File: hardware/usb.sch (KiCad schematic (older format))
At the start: 33 parts, among them J2 USB_B_Micro, U14 FT2232H, U31 93LCxxB, Y1 ABM10-167-12.000MHZ-T3

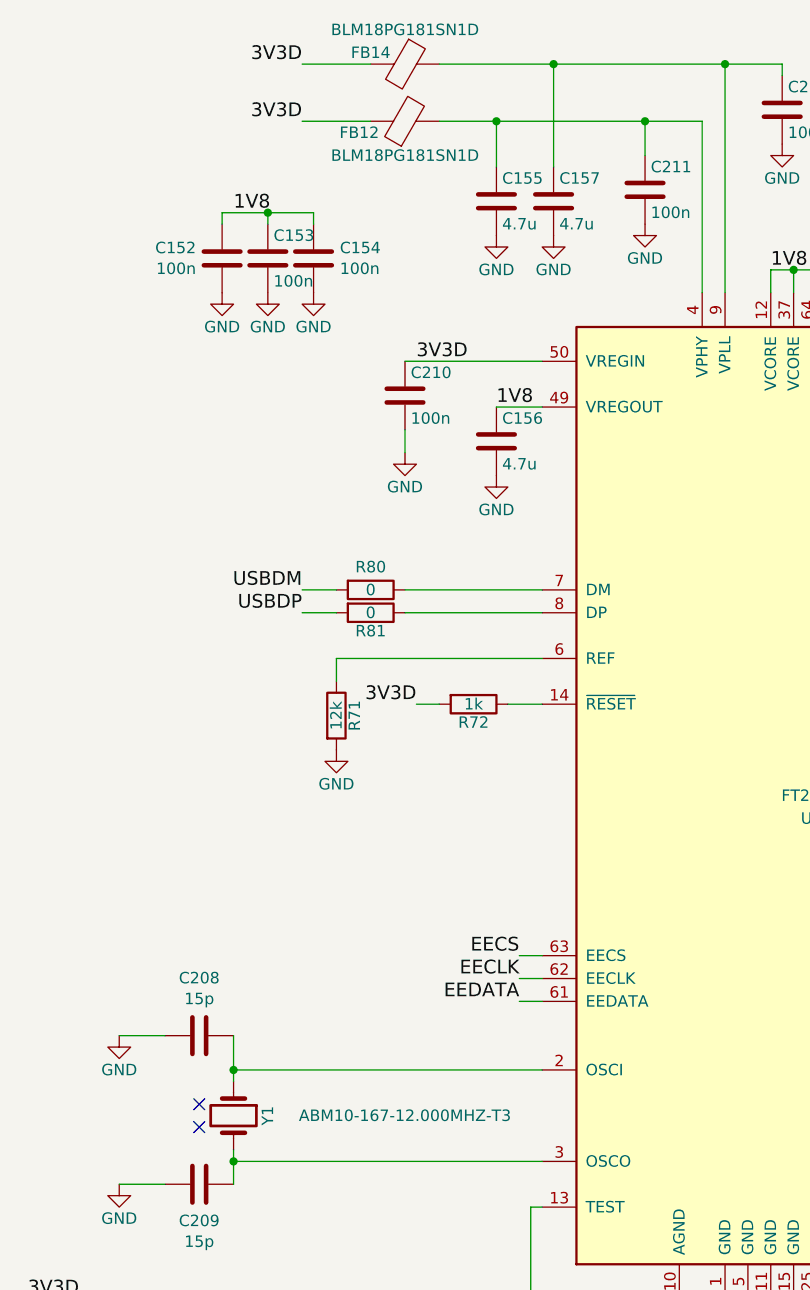
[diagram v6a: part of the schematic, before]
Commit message: Added MFNs to components.
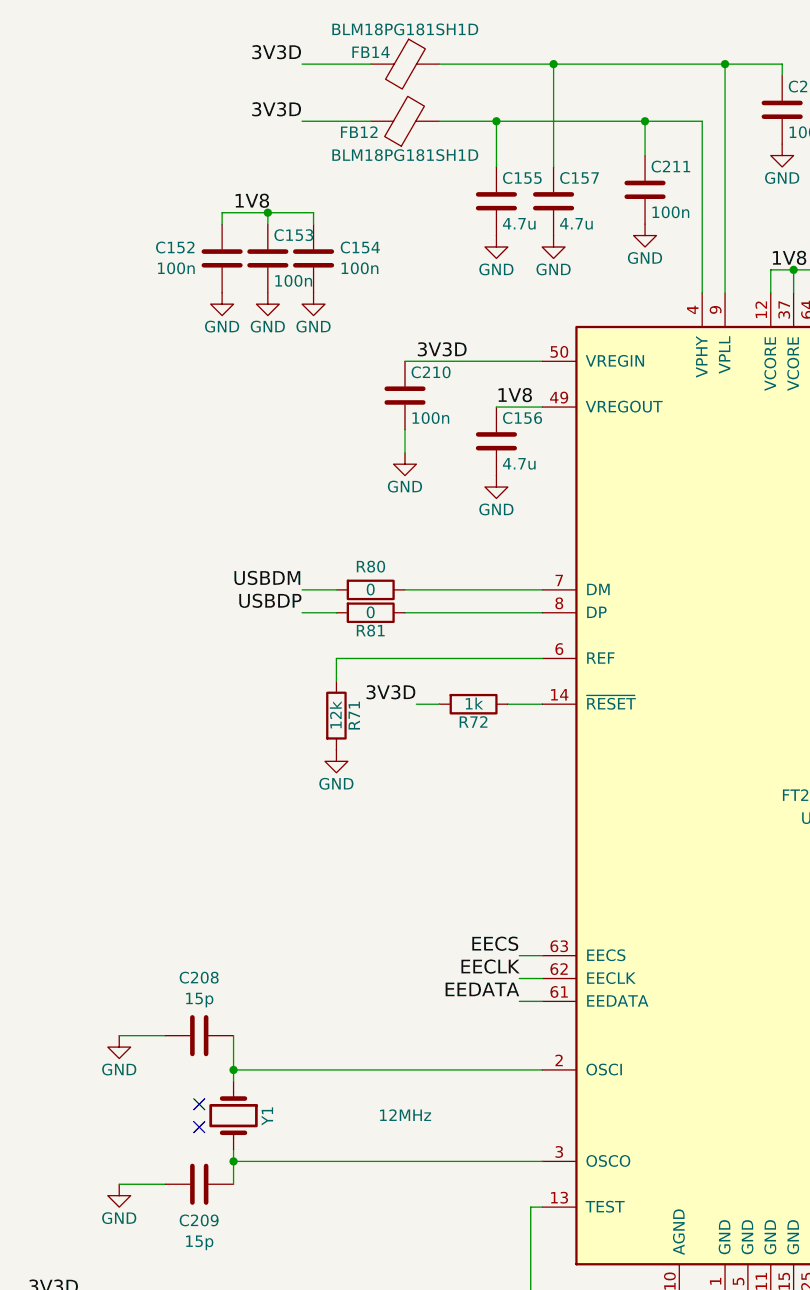
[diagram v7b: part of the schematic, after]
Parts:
- C152, C153, C154, C158, C159, C160, C161, C207, C210, C211, C212: MFN (none) -> CL05B104KO5NNNC
- C155, C156, C157: MFN (none) -> CL10A475KA8NQNC
- C208, C209: MFN (none) -> CGA2B2NP01H150J050BA
- FB12, FB14: value BLM18PG181SN1D -> BLM18PG181SH1D; footprint fmcw:C_0603b -> Inductor_SMD:L_0603_1608Metric; MFN (none) -> BLM18PG181SH1D
- J2: MFN (none) -> 10103594-0001LF
- R71: footprint fmcw:R_0402b -> Resistor_SMD:R_0402_1005Metric; MFN (none) -> ERJ-2RKF1202X
- R72: footprint fmcw:R_0402b -> Resistor_SMD:R_0402_1005Metric; MFN (none) -> ERJ-2RKF1001X
- R73, R83: footprint fmcw:R_0402b -> Resistor_SMD:R_0402_1005Metric; MFN (none) -> ERJ-2RKF1002X
- R79: footprint fmcw:R_0402b -> Resistor_SMD:R_0402_1005Metric; MFN (none) -> ERJ-2RKF2201X
- R80, R81: footprint fmcw:R_0402b -> Resistor_SMD:R_0402_1005Metric; MFN (none) -> ERJ-2GE0R00X
- R82: footprint fmcw:R_0402b -> Resistor_SMD:R_0402_1005Metric; MFN (none) -> ERJ-2GEJ472X
- R84, R85, R88: footprint fmcw:R_0402b -> Resistor_SMD:R_0402_1005Metric; MFN (none) -> ERJ-2GEJ330X
- U14: MFN (none) -> FT2232HL-REEL
- U31: footprint Package_TO_SOT_SMD:SOT-23-6 -> Package_SO:SOIC-8_3.9x4.9mm_P1.27mm; MFN (none) -> 93LC46BT-I/SN
- Y1: value ABM10-167-12.000MHZ-T3 -> 12MHz; MFN (none) -> ABM10-167-12.000MHZ-T3
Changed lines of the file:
@@
 F 0 "R80" V 4300 3350 50  0000 C CNN
 F 1 "0" V 4400 3350 50  0000 C CNN
-F 2 "fmcw:R_0402b" V 4330 3350 30  0001 C CNN
+F 2 "Resistor_SMD:R_0402_1005Metric" V 4330 3350 30  0001 C CNN
 F 3 "" H 4400 3350 30  0000 C CNN
+F 4 "ERJ-2GE0R00X" H 0   0   50  0001 C CNN "MFN"
 	1    4400 3350
 	0    1    1    0
@@
 F 0 "R81" V 4480 3450 50  0000 C CNN
 F 1 "0" V 4400 3450 50  0000 C CNN
-F 2 "fmcw:R_0402b" V 4330 3450 30  0001 C CNN
+F 2 "Resistor_SMD:R_0402_1005Metric" V 4330 3450 30  0001 C CNN
 F 3 "" H 4400 3450 30  0000 C CNN
+F 4 "ERJ-2GE0R00X" H 0   0   50  0001 C CNN "MFN"
 	1    4400 3450
 	0    1    1    0
@@
 F 2 "Capacitor_SMD:C_0402_1005Metric" H 4588 2350 30  0001 C CNN
 F 3 "" H 4550 2500 60  0000 C CNN
+F 4 "CL05B104KO5NNNC" H 0   0   50  0001 C CNN "MFN"
 	1    4550 2500
 	1    0    0    -1
@@
 F 2 "Capacitor_SMD:C_0402_1005Metric" H 6238 1100 30  0001 C CNN
 F 3 "" H 6200 1250 60  0000 C CNN
+F 4 "CL05B104KO5NNNC" H 0   0   50  0001 C CNN "MFN"
 	1    6200 1250
 	1    0    0    -1
@@
 F 2 "Capacitor_SMD:C_0402_1005Metric" H 5638 1450 30  0001 C CNN
 F 3 "" H 5600 1600 60  0000 C CNN
+F 4 "CL05B104KO5NNNC" H 0   0   50  0001 C CNN "MFN"
 	1    5600 1600
 	1    0    0    -1
@@
 F 0 "R84" V 8080 4150 50  0000 C CNN
 F 1 "33" V 8000 4150 50  0000 C CNN
-F 2 "fmcw:R_0402b" V 7930 4150 30  0001 C CNN
+F 2 "Resistor_SMD:R_0402_1005Metric" V 7930 4150 30  0001 C CNN
 F 3 "" H 8000 4150 30  0000 C CNN
+F 4 "ERJ-2GEJ330X" H 0   0   50  0001 C CNN "MFN"
 	1    8000 4150
 	0    1    1    0
@@
 F 0 "R88" V 8480 4250 50  0000 C CNN
 F 1 "33" V 8400 4250 50  0000 C CNN
-F 2 "fmcw:R_0402b" V 8330 4250 30  0001 C CNN
+F 2 "Resistor_SMD:R_0402_1005Metric" V 8330 4250 30  0001 C CNN
 F 3 "" H 8400 4250 30  0000 C CNN
+F 4 "ERJ-2GEJ330X" H 0   0   50  0001 C CNN "MFN"
 	1    8400 4250
 	0    1    1    0
@@
 F 0 "R85" V 8080 4450 50  0000 C CNN
 F 1 "33" V 8000 4450 50  0000 C CNN
-F 2 "fmcw:R_0402b" V 7930 4450 30  0001 C CNN
+F 2 "Resistor_SMD:R_0402_1005Metric" V 7930 4450 30  0001 C CNN
 F 3 "" H 8000 4450 30  0000 C CNN
+F 4 "ERJ-2GEJ330X" H 0   0   50  0001 C CNN "MFN"
 	1    8000 4450
 	0    1    1    0
@@
 P 3800 5650
 F 0 "Y1" H 3800 5800 50  0000 C CNN
-F 1 "ABM10-167-12.000MHZ-T3" V 3800 6400 50  0000 C CNN
+F 1 "12MHz" V 3800 6400 50  0000 C CNN
 F 2 "Crystal:Crystal_SMD_Abracon_ABM10-4Pin_2.5x2.0mm" H 3800 5650 60  0001 C CNN
 F 3 "https://abracon.com/Resonators/ABM10-166-12.000MHz.pdf" H 3800 5650 60  0001 C CNN
+F 4 "ABM10-167-12.000MHZ-T3" H 0   0   50  0001 C CNN "MFN"
 	1    3800 5650
 	0    1    1    0
@@
 F 2 "Capacitor_SMD:C_0402_1005Metric" H 3688 5800 30  0001 C CNN
 F 3 "" H 3650 5950 60  0000 C CNN
+F 4 "CGA2B2NP01H150J050BA" H 0   0   50  0001 C CNN "MFN"
 	1    3650 5950
 	0    1    1    0
@@
 F 2 "Capacitor_SMD:C_0402_1005Metric" H 3688 5150 30  0001 C CNN
 F 3 "" H 3650 5300 60  0000 C CNN
+F 4 "CGA2B2NP01H150J050BA" H 0   0   50  0001 C CNN "MFN"
 	1    3650 5300
 	0    1    1    0
@@
 F 0 "R73" V 1380 4200 50  0000 C CNN
 F 1 "10k" V 1300 4200 50  0000 C CNN
-F 2 "fmcw:R_0402b" V 1230 4200 30  0001 C CNN
+F 2 "Resistor_SMD:R_0402_1005Metric" V 1230 4200 30  0001 C CNN
 F 3 "" H 1300 4200 30  0000 C CNN
+F 4 "ERJ-2RKF1002X" H 0   0   50  0001 C CNN "MFN"
 	1    1300 4200
 	1    0    0    -1
@@
 F 0 "R79" V 1380 4600 50  0000 C CNN
 F 1 "2.2k" V 1300 4600 50  0000 C CNN
-F 2 "fmcw:R_0402b" V 1230 4600 30  0001 C CNN
+F 2 "Resistor_SMD:R_0402_1005Metric" V 1230 4600 30  0001 C CNN
 F 3 "" H 1300 4600 30  0000 C CNN
+F 4 "ERJ-2RKF2201X" H 0   0   50  0001 C CNN "MFN"
 	1    1300 4600
 	1    0    0    -1
@@
 F 2 "Capacitor_SMD:C_0402_1005Metric" H 2488 6550 30  0001 C CNN
 F 3 "" H 2450 6700 60  0000 C CNN
+F 4 "CL05B104KO5NNNC" H 0   0   50  0001 C CNN "MFN"
 	1    2450 6700
 	1    0    0    -1
@@
 P 4550 1300
 F 0 "FB12" V 4500 1500 50  0000 C CNN
-F 1 "BLM18PG181SN1D" V 4400 1300 50  0000 C CNN
-F 2 "fmcw:C_0603b" H 4550 1300 60  0001 C CNN
+F 1 "BLM18PG181SH1D" V 4400 1300 50  0000 C CNN
+F 2 "Inductor_SMD:L_0603_1608Metric" H 4550 1300 60  0001 C CNN
 F 3 "" H 4550 1300 60  0000 C CNN
+F 4 "BLM18PG181SH1D" H 0   0   50  0001 C CNN "MFN"
 	1    4550 1300
 	0    -1   -1   0
@@
 P 4550 1050
 F 0 "FB14" V 4500 900 50  0000 C CNN
-F 1 "BLM18PG181SN1D" V 4400 1050 50  0000 C CNN
-F 2 "fmcw:C_0603b" H 4550 1050 60  0001 C CNN
+F 1 "BLM18PG181SH1D" V 4400 1050 50  0000 C CNN
+F 2 "Inductor_SMD:L_0603_1608Metric" H 4550 1050 60  0001 C CNN
 F 3 "" H 4550 1050 60  0000 C CNN
+F 4 "BLM18PG181SH1D" H 0   0   50  0001 C CNN "MFN"
 	1    4550 1050
 	0    1    1    0
@@
 F 2 "Capacitor_SMD:C_0402_1005Metric" H 7188 1100 30  0001 C CNN
 F 3 "" H 7150 1250 60  0000 C CNN
+F 4 "CL05B104KO5NNNC" H 0   0   50  0001 C CNN "MFN"
 	1    7150 1250
 	1    0    0    -1
@@
 F 2 "Capacitor_SMD:C_0402_1005Metric" H 7438 1100 30  0001 C CNN
 F 3 "" H 7400 1250 60  0000 C CNN
+F 4 "CL05B104KO5NNNC" H 0   0   50  0001 C CNN "MFN"
 	1    7400 1250
 	1    0    0    -1
@@
 F 2 "Capacitor_SMD:C_0402_1005Metric" H 7688 1100 30  0001 C CNN
 F 3 "" H 7650 1250 60  0000 C CNN
+F 4 "CL05B104KO5NNNC" H 0   0   50  0001 C CNN "MFN"
 	1    7650 1250
 	1    0    0    -1
@@
 F 2 "Capacitor_SMD:C_0402_1005Metric" H 7938 1100 30  0001 C CNN
 F 3 "" H 7900 1250 60  0000 C CNN
+F 4 "CL05B104KO5NNNC" H 0   0   50  0001 C CNN "MFN"
 	1    7900 1250
 	1    0    0    -1
@@
 F 2 "Capacitor_SMD:C_0603_1608Metric" H 4988 1500 30  0001 C CNN
 F 3 "" H 4950 1650 60  0000 C CNN
+F 4 "CL10A475KA8NQNC" H 0   0   50  0001 C CNN "MFN"
 	1    4950 1650
 	1    0    0    -1
@@
 F 2 "Capacitor_SMD:C_0603_1608Metric" H 5238 1500 30  0001 C CNN
 F 3 "" H 5200 1650 60  0000 C CNN
+F 4 "CL10A475KA8NQNC" H 0   0   50  0001 C CNN "MFN"
 	1    5200 1650
 	1    0    0    -1
@@
 F 2 "Capacitor_SMD:C_0603_1608Metric" H 4988 2550 30  0001 C CNN
 F 3 "" H 4950 2700 60  0000 C CNN
+F 4 "CL10A475KA8NQNC" H 0   0   50  0001 C CNN "MFN"
 	1    4950 2700
 	1    0    0    -1
@@
 F 0 "R72" V 4930 3850 50  0000 C CNN
 F 1 "1k" V 4850 3850 50  0000 C CNN
-F 2 "fmcw:R_0402b" V 4780 3850 30  0001 C CNN
+F 2 "Resistor_SMD:R_0402_1005Metric" V 4780 3850 30  0001 C CNN
 F 3 "" H 4850 3850 30  0000 C CNN
+F 4 "ERJ-2RKF1001X" H 0   0   50  0001 C CNN "MFN"
 	1    4850 3850
 	0    1    1    0
@@
 F 0 "R71" V 4330 3900 50  0000 C CNN
 F 1 "12k" V 4250 3900 50  0000 C CNN
-F 2 "fmcw:R_0402b" V 4180 3900 30  0001 C CNN
+F 2 "Resistor_SMD:R_0402_1005Metric" V 4180 3900 30  0001 C CNN
 F 3 "" H 4250 3900 30  0000 C CNN
+F 4 "ERJ-2RKF1202X" H 0   0   50  0001 C CNN "MFN"
 	1    4250 3900
 	1    0    0    -1
@@
 F 0 "R82" V 8680 5600 50  0000 C CNN
 F 1 "4.7k" V 8600 5600 50  0000 C CNN
-F 2 "fmcw:R_0402b" V 8530 5600 30  0001 C CNN
+F 2 "Resistor_SMD:R_0402_1005Metric" V 8530 5600 30  0001 C CNN
 F 3 "" H 8600 5600 30  0000 C CNN
+F 4 "ERJ-2GEJ472X " H 0   0   50  0001 C CNN "MFN"
 	1    8600 5600
 	1    0    0    -1
@@
 F 0 "R83" V 8680 5950 50  0000 C CNN
 F 1 "10k" V 8600 5950 50  0000 C CNN
-F 2 "fmcw:R_0402b" V 8530 5950 30  0001 C CNN
+F 2 "Resistor_SMD:R_0402_1005Metric" V 8530 5950 30  0001 C CNN
 F 3 "" H 8600 5950 30  0000 C CNN
+F 4 "ERJ-2RKF1002X" H 0   0   50  0001 C CNN "MFN"
 	1    8600 5950
 	1    0    0    -1
@@
 F 2 "Capacitor_SMD:C_0402_1005Metric" H 3788 1750 30  0001 C CNN
 F 3 "" H 3750 1900 60  0000 C CNN
+F 4 "CL05B104KO5NNNC" H 0   0   50  0001 C CNN "MFN"
 	1    3750 1900
 	1    0    0    -1
@@
 F 2 "Capacitor_SMD:C_0402_1005Metric" H 3988 1750 30  0001 C CNN
 F 3 "" H 3950 1900 60  0000 C CNN
+F 4 "CL05B104KO5NNNC" H 0   0   50  0001 C CNN "MFN"
 	1    3950 1900
 	1    0    0    -1
@@
 F 2 "Capacitor_SMD:C_0402_1005Metric" H 4188 1750 30  0001 C CNN
 F 3 "" H 4150 1900 60  0000 C CNN
+F 4 "CL05B104KO5NNNC" H 0   0   50  0001 C CNN "MFN"
 	1    4150 1900
 	1    0    0    -1
@@
 F 2 "Package_QFP:LQFP-64_10x10mm_P0.5mm" H 6350 4250 50  0001 C CNN
 F 3 "http://www.ftdichip.com/Products/ICs/FT2232H.html" H 6350 4250 50  0001 C CNN
+F 4 "FT2232HL-REEL" H 0   0   50  0001 C CNN "MFN"
 	1    6350 4250
 	1    0    0    -1
@@
 F 0 "U31" H 3750 6800 50  0000 C CNN
 F 1 "93LCxxB" H 3700 7300 50  0000 C CNN
-F 2 "Package_TO_SOT_SMD:SOT-23-6" H 3500 7050 50  0001 C CNN
+F 2 "Package_SO:SOIC-8_3.9x4.9mm_P1.27mm" H 3500 7050 50  0001 C CNN
 F 3 "http://ww1.microchip.com/downloads/en/DeviceDoc/20001749K.pdf" H 3500 7050 50  0001 C CNN
+F 4 "93LC46BT-I/SN" H 3500 7050 50  0001 C CNN "MFN"
 	1    3500 7050
 	1    0    0    -1
@@
 F 2 "Connector_USB:USB_Micro-B_Amphenol_10103594-0001LF_Horizontal" H 1400 2900 50  0001 C CNN
 F 3 "~" H 1400 2900 50  0001 C CNN
+F 4 "10103594-0001LF" H 0   0   50  0001 C CNN "MFN"
 	1    1250 2950
 	1    0    0    -1

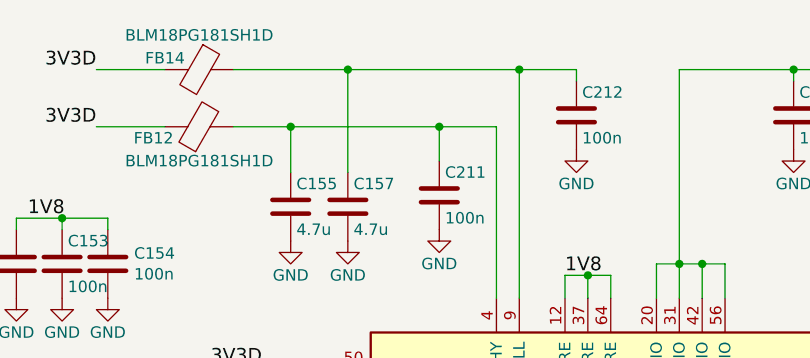
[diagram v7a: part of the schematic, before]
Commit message: Fixed ERC errors.
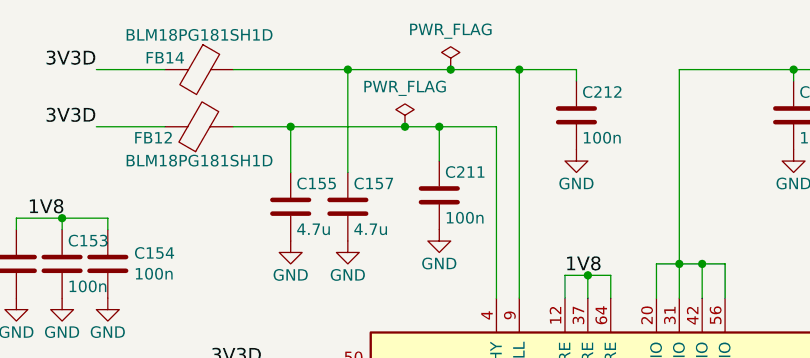
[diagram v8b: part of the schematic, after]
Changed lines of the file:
@@
 	7900 1050 8050 1050
 Wire Wire Line
-	4950 1300 5600 1300
+	4950 1300 5450 1300
 Wire Wire Line
-	5200 1050 5950 1050
+	5200 1050 5650 1050
 Wire Wire Line
 	6250 1950 6350 1950
@@
 NoConn ~ 7550 5650
 NoConn ~ 7550 5950
-Wire Wire Line
-	6650 1050 7150 1050
 Wire Wire Line
 	7550 5750 8600 5750
@@
 Wire Wire Line
 	1250 3400 1250 3450
+$Comp
+L power:PWR_FLAG #FLG0103
+U 1 1 5CF1D020
+P 5650 1050
+F 0 "#FLG0103" H 5650 1125 50  0001 C CNN
+F 1 "PWR_FLAG" H 5650 1224 50  0000 C CNN
+F 2 "" H 5650 1050 50  0001 C CNN
+F 3 "~" H 5650 1050 50  0001 C CNN
+	1    5650 1050
+	1    0    0    -1
+$EndComp
+Connection ~ 5650 1050
+Wire Wire Line
+	5650 1050 5950 1050
+$Comp
+L power:PWR_FLAG #FLG0104
+U 1 1 5CF1D076
+P 5450 1300
+F 0 "#FLG0104" H 5450 1375 50  0001 C CNN
+F 1 "PWR_FLAG" H 5450 1474 50  0000 C CNN
+F 2 "" H 5450 1300 50  0001 C CNN
+F 3 "~" H 5450 1300 50  0001 C CNN
+	1    5450 1300
+	1    0    0    -1
+$EndComp
+Connection ~ 5450 1300
+Wire Wire Line
+	5450 1300 5600 1300
+Wire Wire Line
+	6650 1050 7150 1050
 $EndSCHEMATC
